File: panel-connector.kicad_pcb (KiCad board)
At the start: 2 copper layers, 95.9 x 90.2 mm, 223 parts, among them J1 PC104-8BIT, J10 TEST_1P, J105 MOLEX_FFC-14, J11 TEST_1P, J12 TEST_1P, J13 TEST_1P, J2 PC104PTH, J200 MOLEX_FFC-14, J201 CONN-TAB, J202 CONN-TAB, J203 CONN-TAB, J204 CONN-TAB, J210 MOLEX_FFC-14, J211 CONN-TAB, J212 CONN-TAB, J213 CONN-TAB, J214 CONN-TAB, J220 MOLEX_FFC-14, J221 CONN-TAB, J222 CONN-TAB, J223 CONN-TAB, J224 CONN-TAB, J230 MOLEX_FFC-14, J231 CONN-TAB, J232 CONN-TAB, J233 CONN-TAB, J234 CONN-TAB, J3 PC104PTH, J4 PC104PTH, J5 PC104PTH, J6 OEM719, J7 B3B-XH-A(LF)(SN), J8 TEST_1P, J9 TEST_1P, U100 SPV1040, U110 SPV1040, U120 SPV1040, U130 SPV1040, U140 SPV1040, U150 SPV1040, U160 SPV1040, U170 SPV1040, U200 ADG728, U210 ADG728, U220 ADG728, U230 ADG728

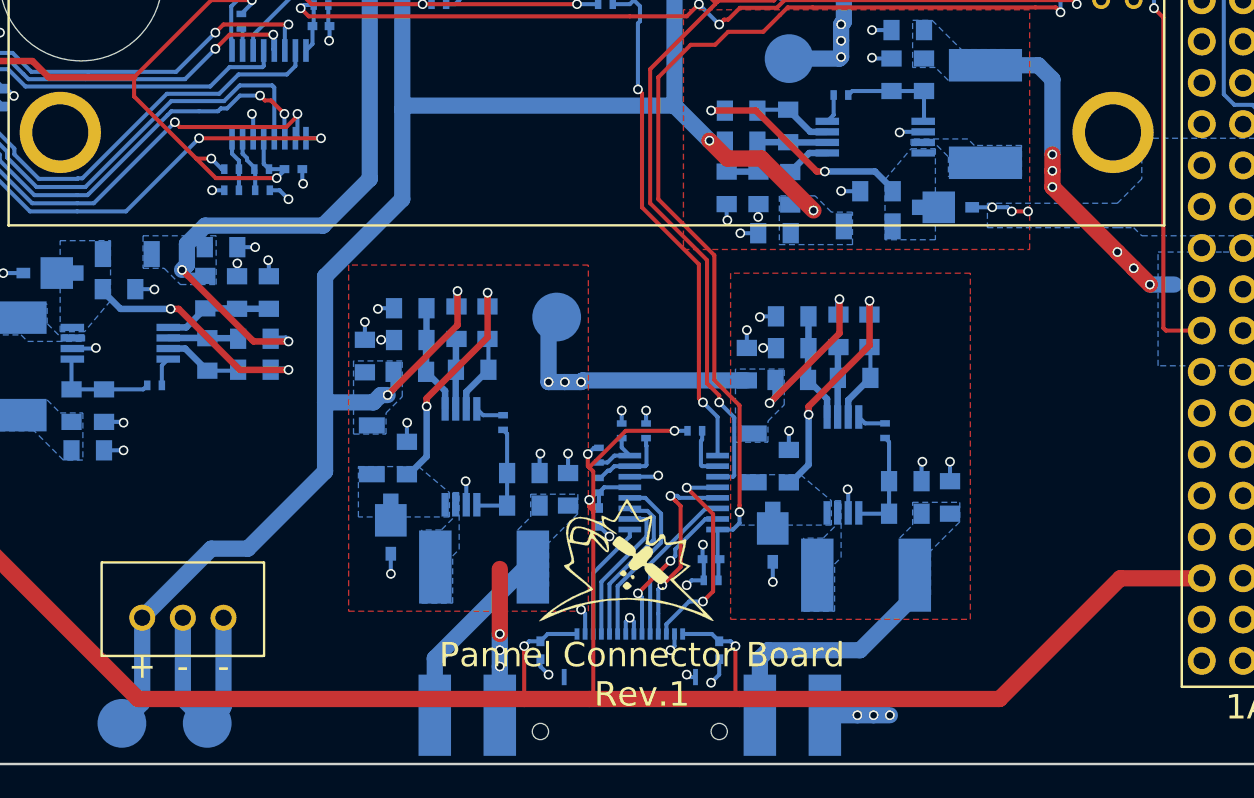
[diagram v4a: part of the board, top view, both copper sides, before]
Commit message: moved DC connection to eps board inorder to avoid RBF switch above on the eps board
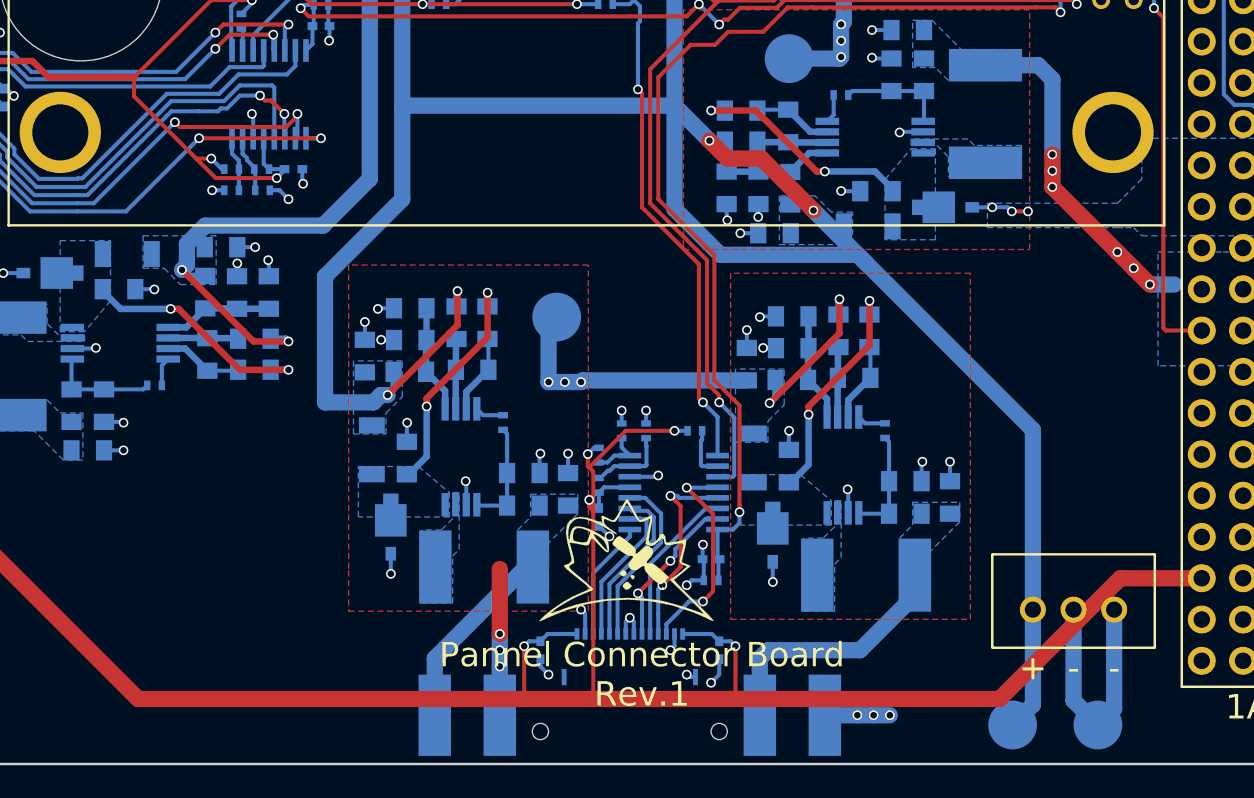
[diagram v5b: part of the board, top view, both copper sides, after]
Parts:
- moved J7 54.8 mm to (180.3, 125.5)
- moved J12 54.8 mm to (176.6, 132.6)
- moved J13 54.8 mm to (181.8, 132.6)
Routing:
- net /MPPT_X+_1/VOUT+: track 171.5 -> 202.6 mm
- net GND: track 151.6 -> 152.8 mm
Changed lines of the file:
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@@
   (general
     (links 473)
-    (no_connects 8)
+    (no_connects 9)
     (area 83.114286 22.899999 253.885715 168.15)
     (thickness 1.6)
     (drawings 180)
-    (tracks 1740)
+    (tracks 1743)
     (zones 0)
     (modules 223)
@@
   )
   (layers
-    (0 F.Cu signal hide)
+    (0 F.Cu signal)
     (31 B.Cu signal)
     (32 B.Adhes user)
@@
   )
   (setup
-    (last_trace_width 0.25)
+    (last_trace_width 1)
     (user_trace_width 0.1524)
     (user_trace_width 0.4)
@@
   )
   (module SFUSat:B3B-XH-A (layer F.Cu)
-    (at 125.5 126)
+    (at 180.3 125.5)
     (fp_text reference J7 (at -6.5 0 90) (layer F.SilkS) hide
       (effects (font (size 1 1) (thickness 0.15)))
@@
   )
   (module SFUSat:Measurement_Point_Round-SMD-Pad_Big (layer B.Cu)
-    (at 121.75 132.5)
+    (at 176.55 132.6)
     (descr "Mesurement Point, Round, SMD Pad, DM 3mm,")
     (tags "Mesurement Point Round SMD Pad 3mm")
@@
   )
   (module SFUSat:Measurement_Point_Round-SMD-Pad_Big (layer B.Cu)
-    (at 127 132.5)
+    (at 181.8 132.6)
     (descr "Mesurement Point, Round, SMD Pad, DM 3mm,")
     (tags "Mesurement Point Round SMD Pad 3mm")
@@
     (effects (font (size 1 1) (thickness 0.15)) (justify mirror))
   )
-  (gr_text 2xx (at 164.5 66.4 360) (layer B.SilkS)
+  (gr_text 2xx (at 164.5 66.4) (layer B.SilkS)
     (effects (font (size 1.5 1.5) (thickness 0.3)) (justify mirror))
   )
@@
     (effects (font (size 1.5 1.5) (thickness 0.3)))
   )
-  (gr_text - (at 128 129) (layer F.SilkS)
+  (gr_text - (at 182.8 129.1) (layer F.SilkS)
     (effects (font (size 1.5 1.5) (thickness 0.3)))
   )
-  (gr_text - (at 125.5 129) (layer F.SilkS)
+  (gr_text - (at 180.3 129.1) (layer F.SilkS)
     (effects (font (size 1.5 1.5) (thickness 0.3)))
   )
-  (gr_text + (at 123 129) (layer F.SilkS)
+  (gr_text + (at 177.8 129.1) (layer F.SilkS)
     (effects (font (size 1.5 1.5) (thickness 0.3)))
   )
@@
   )
   (gr_line (start 200.89 135) (end 200.89 44.83) (layer Edge.Cuts) (width 0.15))
+  (segment (start 182.8 125.5) (end 182.8 131.6) (width 1) (layer B.Cu) (net 51))
+  (segment (start 180.3 131.1) (end 180.3 125.5) (width 1) (layer B.Cu) (net 51))
   (segment (start 134.75 62.5) (end 141.5 62.5) (width 0.25) (layer B.Cu) (net 51))
   (segment (start 141.5 62.5) (end 141.6 62.6) (width 0.25) (layer B.Cu) (net 51))
@@
   (segment (start 141.3 72.8) (end 142 73.5) (width 0.25) (layer B.Cu) (net 51))
   (via (at 142 73.5) (size 0.6) (drill 0.4) (layers F.Cu B.Cu) (net 51))
-  (segment (start 125.5 126) (end 125.5 131) (width 1) (layer B.Cu) (net 51))
-  (segment (start 125.5 131) (end 127 132.5) (width 1) (layer B.Cu) (net 51))
-  (segment (start 128 126) (end 128 131.5) (width 1) (layer B.Cu) (net 51))
-  (segment (start 128 131.5) (end 127 132.5) (width 1) (layer B.Cu) (net 51))
+  (segment (start 180.3 131.1) (end 181.8 132.6) (width 1) (layer B.Cu) (net 51))
+  (segment (start 182.8 131.6) (end 181.8 132.6) (width 1) (layer B.Cu) (net 51))
   (via (at 196.75 78.75) (size 0.6) (drill 0.4) (layers F.Cu B.Cu) (net 51))
   (segment (start 198.025 80.025) (end 196.75 78.75) (width 0.25) (layer F.Cu) (net 51))
@@
   (via (at 164.3 85.9) (size 0.6) (drill 0.4) (layers F.Cu B.Cu) (net 65))
   (via (at 157.9 81.6) (size 0.6) (drill 0.4) (layers F.Cu B.Cu) (net 65))
-  (segment (start 123 126) (end 123 131.25) (width 1) (layer B.Cu) (net 66))
-  (segment (start 123 131.25) (end 121.75 132.5) (width 1) (layer B.Cu) (net 66))
-  (segment (start 134.25 112.75) (end 134.25 117) (width 1) (layer B.Cu) (net 66))
-  (segment (start 134.25 117) (end 129.5 121.75) (width 1) (layer B.Cu) (net 66))
-  (segment (start 129.5 121.75) (end 127.25 121.75) (width 1) (layer B.Cu) (net 66))
-  (segment (start 127.25 121.75) (end 123 126) (width 1) (layer B.Cu) (net 66))
+  (segment (start 177.8 114.443796) (end 167.556204 104.2) (width 1) (layer B.Cu) (net 66))
+  (segment (start 167.556204 104.2) (end 164.3 100.943796) (width 1) (layer B.Cu) (net 66))
+  (segment (start 155.75 100.85) (end 158.568797 103.668797) (width 1) (layer B.Cu) (net 66))
+  (segment (start 158.568797 103.668797) (end 167.025001 103.668797) (width 1) (layer B.Cu) (net 66))
+  (segment (start 167.025001 103.668797) (end 167.556204 104.2) (width 1) (layer B.Cu) (net 66))
+  (segment (start 155.75 94.493796) (end 155.75 100.85) (width 1) (layer B.Cu) (net 66))
+  (segment (start 177.8 125.5) (end 177.8 114.443796) (width 1) (layer B.Cu) (net 66))
+  (segment (start 177.8 131.35) (end 177.8 125.5) (width 1) (layer B.Cu) (net 66))
+  (segment (start 177.8 131.35) (end 176.55 132.6) (width 1) (layer B.Cu) (net 66))
   (segment (start 139 87.75) (end 139 94.75) (width 1) (layer B.Cu) (net 66))
   (segment (start 139 94.75) (end 139 100.25) (width 1) (layer B.Cu) (net 66))

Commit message: generated gerbers
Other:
- rule pad_to_mask_clearance: 0 -> 0.03
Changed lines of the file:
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@@
     (pad_size 5 5)
     (pad_drill 3.45)
-    (pad_to_mask_clearance 0)
+    (pad_to_mask_clearance 0.03)
+    (pad_to_paste_clearance -0.03)
     (aux_axis_origin 20 140)
     (grid_origin 105 135)

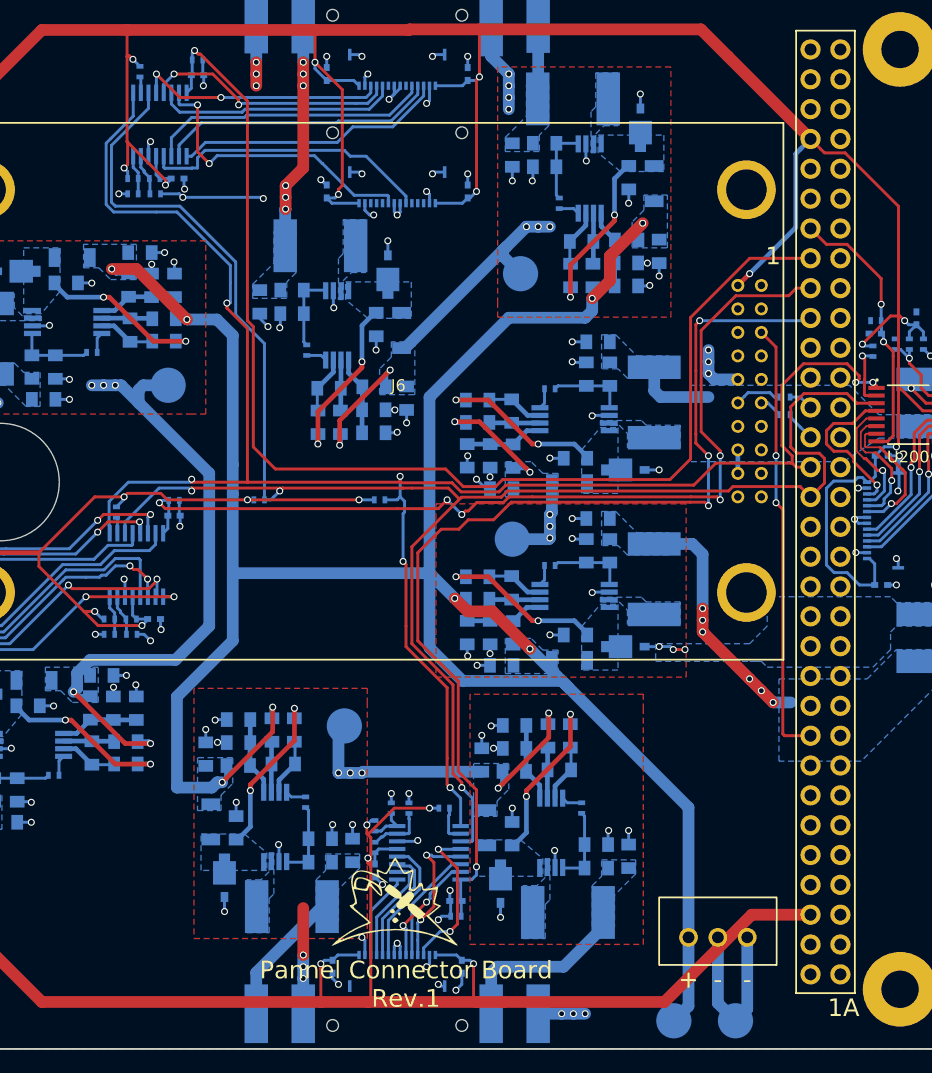
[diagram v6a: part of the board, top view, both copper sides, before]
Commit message: fixed 3v3 trace collision and GPS PTH grounded
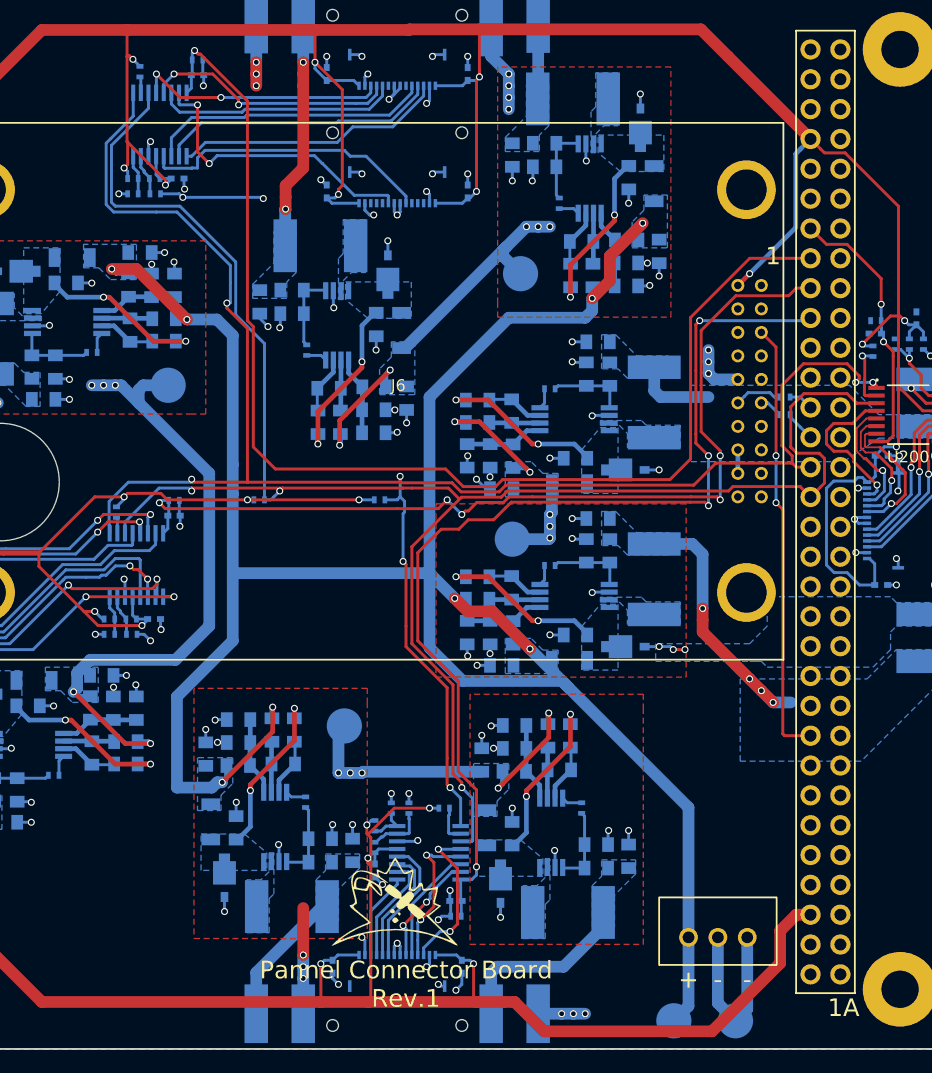
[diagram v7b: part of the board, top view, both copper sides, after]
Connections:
- J6 pad : (no net) -> GND
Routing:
- net /3V3: track 502.2 -> 505.9 mm
- net /MPPT_Y-_2/PV+: vias 6 -> 2
- net /MPPT_X+_1/PV+: vias 6 -> 4
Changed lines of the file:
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@@
   (general
     (links 473)
-    (no_connects 9)
+    (no_connects 8)
     (area 83.114286 22.899999 253.885715 168.15)
     (thickness 1.6)
     (drawings 180)
-    (tracks 1743)
+    (tracks 1742)
     (zones 0)
     (modules 223)
@@
   )
   (setup
-    (last_trace_width 1)
+    (last_trace_width 0.25)
     (user_trace_width 0.1524)
     (user_trace_width 0.4)
@@
     (fp_line (start 0 -45.7) (end 71.1 -45.7) (layer F.SilkS) (width 0.15))
     (fp_line (start 0 0) (end 0 -45.7) (layer F.SilkS) (width 0.15))
-    (pad "" thru_hole circle (at 3.18 -5.72) (size 5 5) (drill 3.45) (layers *.Cu *.Mask))
-    (pad "" thru_hole circle (at 3.18 -40.01) (size 5 5) (drill 3.45) (layers *.Mask B.Cu))
-    (pad "" thru_hole circle (at 67.95 -40.01) (size 5 5) (drill 3.45) (layers *.Cu *.Mask))
-    (pad "" thru_hole circle (at 67.95 -5.72) (size 5 5) (drill 3.45) (layers *.Cu *.Mask))
+    (pad "" thru_hole circle (at 3.18 -5.72) (size 5 5) (drill 3.45) (layers *.Cu *.Mask)
+      (net 51 GND))
+    (pad "" thru_hole circle (at 3.18 -40.01) (size 5 5) (drill 3.45) (layers *.Cu *.Mask)
+      (net 51 GND))
+    (pad "" thru_hole circle (at 67.95 -40.01) (size 5 5) (drill 3.45) (layers *.Cu *.Mask)
+      (net 51 GND))
+    (pad "" thru_hole circle (at 67.95 -5.72) (size 5 5) (drill 3.45) (layers *.Cu *.Mask)
+      (net 51 GND))
     (pad 1 thru_hole circle (at 69.22 -31.86) (size 1.1 1.1) (drill 0.64) (layers *.Cu *.Mask)
       (net 160 "Net-(J6-Pad1)"))
@@
     (tags "capacitor 0402")
     (attr smd)
-    (fp_text reference C203 (at 4.25 0) (layer B.SilkS)
+    (fp_text reference C203 (at -0.55 -2.4 90) (layer B.SilkS)
       (effects (font (size 1 1) (thickness 0.15)) (justify mirror))
     )
@@
   (via (at 183 103.5) (size 0.6) (drill 0.4) (layers F.Cu B.Cu) (net 64))
   (segment (start 179 99.5) (end 183 103.5) (width 1) (layer F.Cu) (net 64))
-  (via (at 179 99.5) (size 0.6) (drill 0.4) (layers F.Cu B.Cu) (net 64))
-  (via (at 179 98.5) (size 0.6) (drill 0.4) (layers F.Cu B.Cu) (net 64))
   (via (at 179 97.5) (size 0.6) (drill 0.4) (layers F.Cu B.Cu) (net 64))
   (segment (start 179 92.877396) (end 179 97.5) (width 1) (layer B.Cu) (net 64))
@@
   (segment (start 143.5 62.5) (end 143.5 61.5) (width 1) (layer F.Cu) (net 76))
   (segment (start 143.5 63.5) (end 143.5 62.5) (width 1) (layer F.Cu) (net 76))
-  (via (at 143.5 61.5) (size 0.6) (drill 0.4) (layers F.Cu B.Cu) (net 76))
-  (via (at 143.5 62.5) (size 0.6) (drill 0.4) (layers F.Cu B.Cu) (net 76))
   (segment (start 143.4652 66.6184) (end 143.4652 63.5348) (width 1) (layer B.Cu) (net 76))
   (segment (start 143.4652 63.5348) (end 143.5 63.5) (width 1) (layer B.Cu) (net 76))
   (via (at 143.5 63.5) (size 0.6) (drill 0.4) (layers F.Cu B.Cu) (net 76))
-  (via (at 145 53) (size 0.6) (drill 0.4) (layers F.Cu B.Cu) (net 76))
-  (via (at 145 52) (size 0.6) (drill 0.4) (layers F.Cu B.Cu) (net 76))
   (segment (start 145 47.745792) (end 145 51) (width 1) (layer B.Cu) (net 76))
   (via (at 145 51) (size 0.6) (drill 0.4) (layers F.Cu B.Cu) (net 76))
@@
   (segment (start 135.55 50.8) (end 135.55 52.025) (width 0.25) (layer B.Cu) (net 80))
   (segment (start 135.55 52.025) (end 135.475 52.1) (width 0.25) (layer B.Cu) (net 80))
+  (segment (start 159.75 131.000001) (end 162.000001 131.000001) (width 1) (layer F.Cu) (net 81))
+  (segment (start 185.6 127.7) (end 185.6 124.943777) (width 1) (layer F.Cu) (net 81))
+  (segment (start 162.000001 131.000001) (end 162.000003 130.999999) (width 1) (layer F.Cu) (net 81))
+  (segment (start 162.000003 130.999999) (end 162.999999 130.999999) (width 1) (layer F.Cu) (net 81))
+  (segment (start 185.6 124.943777) (end 186.973777 123.57) (width 1) (layer F.Cu) (net 81))
+  (segment (start 162.999999 130.999999) (end 165.5 133.5) (width 1) (layer F.Cu) (net 81))
+  (segment (start 165.5 133.5) (end 179.8 133.5) (width 1) (layer F.Cu) (net 81))
+  (segment (start 179.8 133.5) (end 185.6 127.7) (width 1) (layer F.Cu) (net 81))
+  (segment (start 186.973777 123.57) (end 188.19 123.57) (width 1) (layer F.Cu) (net 81))
   (segment (start 113.6 94.6) (end 113.65 94.55) (width 0.25) (layer B.Cu) (net 81))
   (segment (start 113.65 94.55) (end 114.5 94.55) (width 0.25) (layer B.Cu) (net 81))
@@
   (segment (start 156.55 114.5) (end 155.75 114.5) (width 0.25) (layer B.Cu) (net 81))
   (via (at 155.75 114.5) (size 0.6) (drill 0.4) (layers F.Cu B.Cu) (net 81))
-  (segment (start 162.000001 131.000001) (end 159.75 131.000001) (width 1) (layer F.Cu) (net 81))
   (segment (start 159.5 127.75) (end 159.5 130.750001) (width 0.25) (layer F.Cu) (net 81))
   (segment (start 159.5 130.750001) (end 159.75 131.000001) (width 0.25) (layer F.Cu) (net 81))
@@
   (segment (start 146 51.55) (end 146 51) (width 0.25) (layer B.Cu) (net 81))
   (via (at 146 51) (size 0.6) (drill 0.4) (layers F.Cu B.Cu) (net 81))
-  (segment (start 188.19 123.57) (end 183.179998 123.57) (width 1) (layer F.Cu) (net 81))
-  (segment (start 183.179998 123.57) (end 175.749999 130.999999) (width 1) (layer F.Cu) (net 81))
-  (segment (start 175.749999 130.999999) (end 162.000003 130.999999) (width 1) (layer F.Cu) (net 81))
-  (segment (start 162.000003 130.999999) (end 162.000001 131.000001) (width 1) (layer F.Cu) (net 81))
   (segment (start 181.16 50.5) (end 188.19 57.53) (width 1) (layer F.Cu) (net 81))
   (segment (start 122.750001 131.000001) (end 109.499999 117.749999) (width 1) (layer F.Cu) (net 81))
@@
   (segment (start 199 87.472947) (end 199 86.5) (width 0.25) (layer B.Cu) (net 182))
   (via (at 199 86.5) (size 0.6) (drill 0.4) (layers F.Cu B.Cu) (net 182))
+  (segment (start 125.010147 95.510147) (end 125.310146 95.810146) (width 0.25) (layer F.Cu) (net 183))
+  (segment (start 132.164121 95.810146) (end 132.550003 95.424264) (width 0.25) (layer F.Cu) (net 183))
+  (segment (start 125.310146 95.810146) (end 132.164121 95.810146) (width 0.25) (layer F.Cu) (net 183))
+  (segment (start 132.550003 95.424264) (end 132.550003 95) (width 0.25) (layer F.Cu) (net 183))
   (segment (start 132.550003 95) (end 132.550003 96.374997) (width 0.25) (layer B.Cu) (net 183))
   (segment (start 132.550003 96.374997) (end 132.425 96.5) (width 0.25) (layer B.Cu) (net 183))
-  (segment (start 125.010147 95.510147) (end 125.310146 95.810146) (width 0.25) (layer F.Cu) (net 183))
-  (segment (start 125.310146 95.810146) (end 131.864856 95.810146) (width 0.25) (layer F.Cu) (net 183))
-  (segment (start 131.864856 95.810146) (end 132.550003 95.124999) (width 0.25) (layer F.Cu) (net 183))
   (segment (start 132.550003 95.124999) (end 132.550003 95) (width 0.25) (layer F.Cu) (net 183))
   (via (at 132.550003 95) (size 0.6) (drill 0.4) (layers F.Cu B.Cu) (net 183))
@@
       (pts
         (xy 189.5 103.5) (xy 193 103.5) (xy 195.5 101) (xy 200 101) (xy 200 103)
-        (xy 192.5 110.5) (xy 185.5 110.5) (xy 185.5 103.5)
+        (xy 192.5 110.5) (xy 182.2 110.5) (xy 182.2 103.5)
       )
     )
